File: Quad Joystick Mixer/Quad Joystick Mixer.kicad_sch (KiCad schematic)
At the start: 18 parts, among them J1 Conn_01x02_Pin, U1 LM338-TO-220, U2 LM2990SX-12

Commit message: workign on draft of PSU circuit--thinking about making it onto its own board
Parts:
- removed J1: Conn_01x02_Pin, symbol Connector:Conn_01x02_Pin
- added C10, C11, C9: 2200uF, symbol Device:C_Polarized_US
- added C12: 10uF, symbol Device:C_Polarized_US
- added C13: 0.1uF, symbol Device:C
- added C8: 2220uF, symbol Device:C_Polarized_US
- added D5, D6, D7: B350, Diode_SMD:D_SMC, symbol Diode:B350
- added J1: Barrel_Jack_Switch, Eyewool Connectors:Love My Switches 2.1MM PCB Mount DC Jack, symbol Connector:Barrel_Jack_Switch
- added R5, R6: 10k, symbol Device:R_US
- added SW1: SW_SPST, symbol Switch:SW_SPST
- C7: value C -> 0.1uF
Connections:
- net +12V: now also D7.1 (K), R6.1
- net Earth: now also C1.1, C10.1, C11.1, C12.1, C13.2, C8.2, C9.2, D6.1 (K), D7.2 (A), J1.1, R5.2, R6.2; no longer C1.2
- net at D1.1 (K), D4.2 (A): now also SW1.2 (B)
- net at D1.2 (A), R2.1: now also C10.2, C11.2
- net at C2.1, R2.2, U2.2 (IN): now also C1.2, D5.2 (A); no longer C1.1
- net -12V: now reaches U2.3 (OUT)
- net -12V: now also C12.2, C13.1, D5.1 (K), D6.2 (A), R5.1
- net at D4.1 (K), R1.1: now also C8.1, C9.1
- new net: J1.2, SW1.1 (A)
- no-connect marks 0 -> 1
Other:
- note removed: "todo: verify input connector"
- moved on the sheet: C1, C2, C3, C4, C5, C6, C7, D1, D2, D3, D4, R1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

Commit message: progress on PSU layout
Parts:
- removed C12, C5, C6: 10uF, symbol Device:C_Polarized_US
- removed SW1: SW_SPST, symbol Switch:SW_SPST
- added C12, C14, C5, C6: 10uF, Capacitor_SMD:C_0805_2012Metric_Pad1.18x1.45mm_HandSolder, symbol Device:C
- added C15, C19, C20, C21, C22, C23: 0.1uF, Capacitor_SMD:C_0805_2012Metric_Pad1.18x1.45mm_HandSolder, symbol Device:C
- added C16: 100pF, Capacitor_SMD:C_0805_2012Metric_Pad1.18x1.45mm_HandSolder, symbol Device:C
- added C17, C18: 22uF, Capacitor_SMD:C_1206_3216Metric_Pad1.33x1.80mm_HandSolder, symbol Device:C
- added D10, D8, D9: LED, LED_THT:LED_D3.0mm_FlatTop, symbol Device:LED
- added F1, F2, F3: Polyfuse, Fuse:Fuse_1206_3216Metric_Pad1.42x1.75mm_HandSolder, symbol Device:Polyfuse
- added J1: B6B-XH-A, Eyewool Connectors:B6B-XH-A, symbol Connector:Conn_01x06_Pin
- added L1: 10uH, Inductor_SMD:L_Abracon_ASPI-0630LR, symbol Device:L
- added L2, L3, L4: L_Ferrite, Inductor_SMD:L_0805_2012Metric_Pad1.15x1.40mm_HandSolder, symbol Device:L_Ferrite
- added R10, R9: 0.5R, Resistor_SMD:R_2512_6332Metric_Pad1.40x3.35mm_HandSolder, symbol Device:R_US
- added R11, R12: 10k, Resistor_SMD:R_0805_2012Metric_Pad1.20x1.40mm_HandSolder, symbol Device:R_US
- added R13: 300, Resistor_SMD:R_0805_2012Metric_Pad1.20x1.40mm_HandSolder, symbol Device:R_US
- added R7: 157k, Resistor_SMD:R_0805_2012Metric_Pad1.20x1.40mm_HandSolder, symbol Device:R_US
- added R8: 30k, Resistor_SMD:R_0805_2012Metric_Pad1.20x1.40mm_HandSolder, symbol Device:R_US
- added SW1: SW_DPDT_x2, Eyewool Switches:Taiway DPDT, symbol Switch:SW_DPDT_x2
- added U3: AP63200WU, Package_TO_SOT_SMD:TSOT-23-6, symbol Regulator_Switching:AP63200WU
- C1, C3: footprint (none) -> Capacitor_THT:CP_Radial_D8.0mm_P3.50mm; DK PN (none) -> 1189-2327-ND; MPN (none) -> 50ZLH100MEFC8X11.5
- C10, C11, C9: footprint (none) -> Capacitor_THT:C_Radial_D16.0mm_H25.0mm_P7.50mm; DK PN (none) -> 1189-2266-ND; MPN (none) -> 35ZLH2200MEFC16X25
- C13, C7: footprint (none) -> Capacitor_SMD:C_0805_2012Metric_Pad1.18x1.45mm_HandSolder; DK PN (none) -> 1276-1003-1-ND; MPN (none) -> CL21B104KBCNNNC
- C2, C4: footprint (none) -> Capacitor_SMD:C_0805_2012Metric_Pad1.18x1.45mm_HandSolder; DK PN (none) -> 1276-1029-1-ND; MPN (none) -> CL21B105KBFNNNE
- C8: value 2220uF -> 2200uF; footprint (none) -> Capacitor_THT:C_Radial_D16.0mm_H25.0mm_P7.50mm; DK PN (none) -> 1189-2266-ND; MPN (none) -> 35ZLH2200MEFC16X25
- D1, D2, D3, D4, D5, D6, D7: footprint Diode_SMD:D_SMC -> Diode_SMD:D_SMA_Handsoldering; DK PN (none) -> B350A-FDICT-ND; MPN (none) -> B350A-13-F
- R1, R2: value 1R -> 0.5R; footprint (none) -> Resistor_SMD:R_2512_6332Metric_Pad1.40x3.35mm_HandSolder; DK PN (none) -> CSRN2512FKR500CT-ND; MPN (none) -> CSRN2512FKR500
- R3, R4, R5, R6: footprint (none) -> Resistor_SMD:R_0805_2012Metric_Pad1.20x1.40mm_HandSolder
- U2: value LM2990SX-12 -> LM2990T-12/NOPB; footprint (none) -> Package_TO_SOT_THT:TO-220-3_Vertical
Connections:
- net +12V: now also C14.1, C15.1, C5.1, L4.1, U3.2 (EN), U3.3 (IN)
- net -12V: now also C12.1, L2.1
- net Earth: now also C12.2, C14.2, C15.2, C17.2, C18.2, C19.2, C21.2, C22.2, C23.2, C5.2, C6.2, J1.2 (Pin_2), J1.4 (Pin_4), J1.6 (Pin_6), R11.2, R12.2, R13.2, R8.2, U3.4 (GND)
- net at D1.1 (K), D4.2 (A): now also SW1.1 (A), SW1.4 (A)
- net at C10.2, C11.2, R2.1: now also R10.2; no longer D1.2 (A)
- net at D3.2 (A), R3.2, R4.1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: now also C6.1
- net at J1.2: now also SW1.2 (B), SW1.5 (B)
- net at C8.1, C9.1, R1.1: now also R9.2; no longer D4.1 (K)
- new net: D1.2 (A), R10.1
- new net: D8.1 (K), R11.1
- new net: C16.2, R7.2, R8.1, U3.1 (FB)
- new net: D4.1 (K), R9.1
- new net: C23.1, F3.1, L4.2
- new net: D8.2 (A), F3.2, J1.5 (Pin_5)
- new net: C20.2, L1.1, U3.5 (SW)
- new net: C20.1, U3.6 (BST)
- new net: C21.1, F1.1, L2.2
- new net: C22.1, F2.1, L3.2
- new net: D9.2 (A), F2.2, J1.3 (Pin_3)
- new net: D10.1 (K), F1.2, J1.1 (Pin_1)
- new net: D10.2 (A), R12.1
- new net: D9.1 (K), R13.1
- new net +5V: C16.1, C17.1, C18.1, C19.1, L1.2, L3.1, R7.1
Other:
- moved on the sheet: C1, C10, C11, C13, C2, C3, C4, C7, C8, C9, D1, D2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

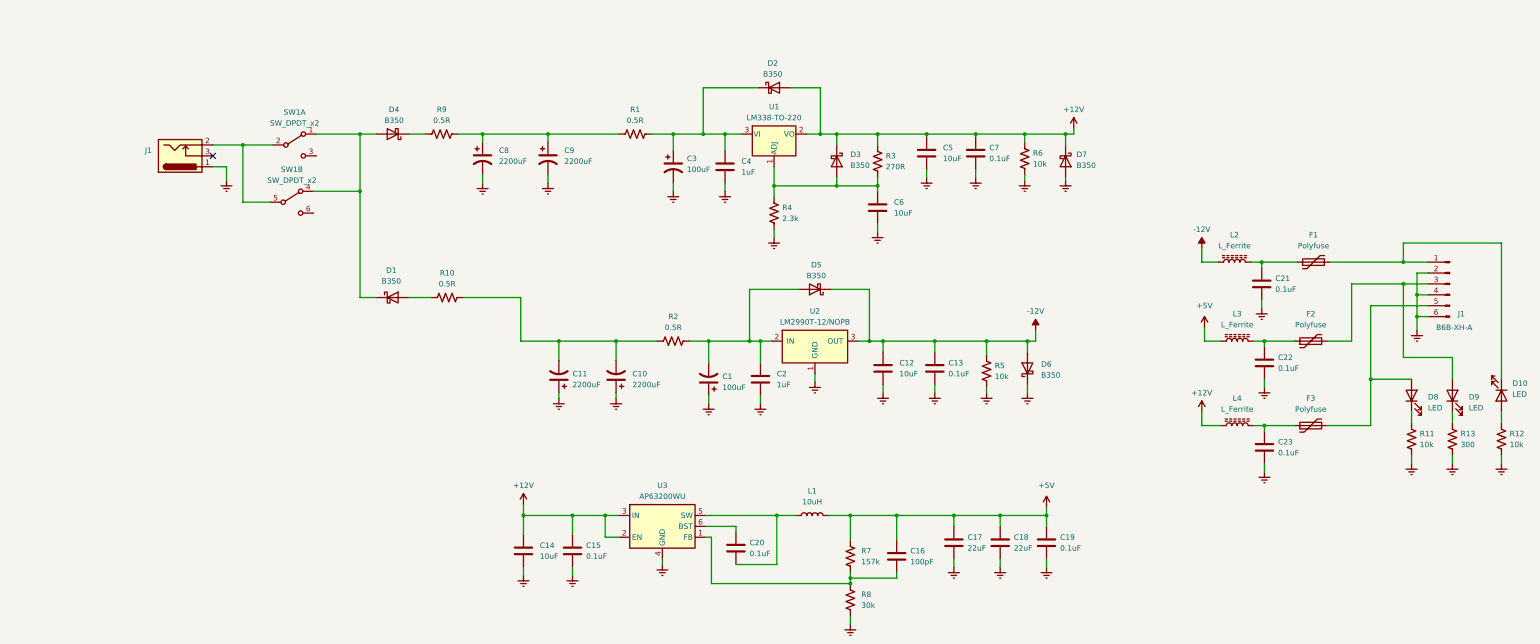
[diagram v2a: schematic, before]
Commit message: clean up power supply schematic
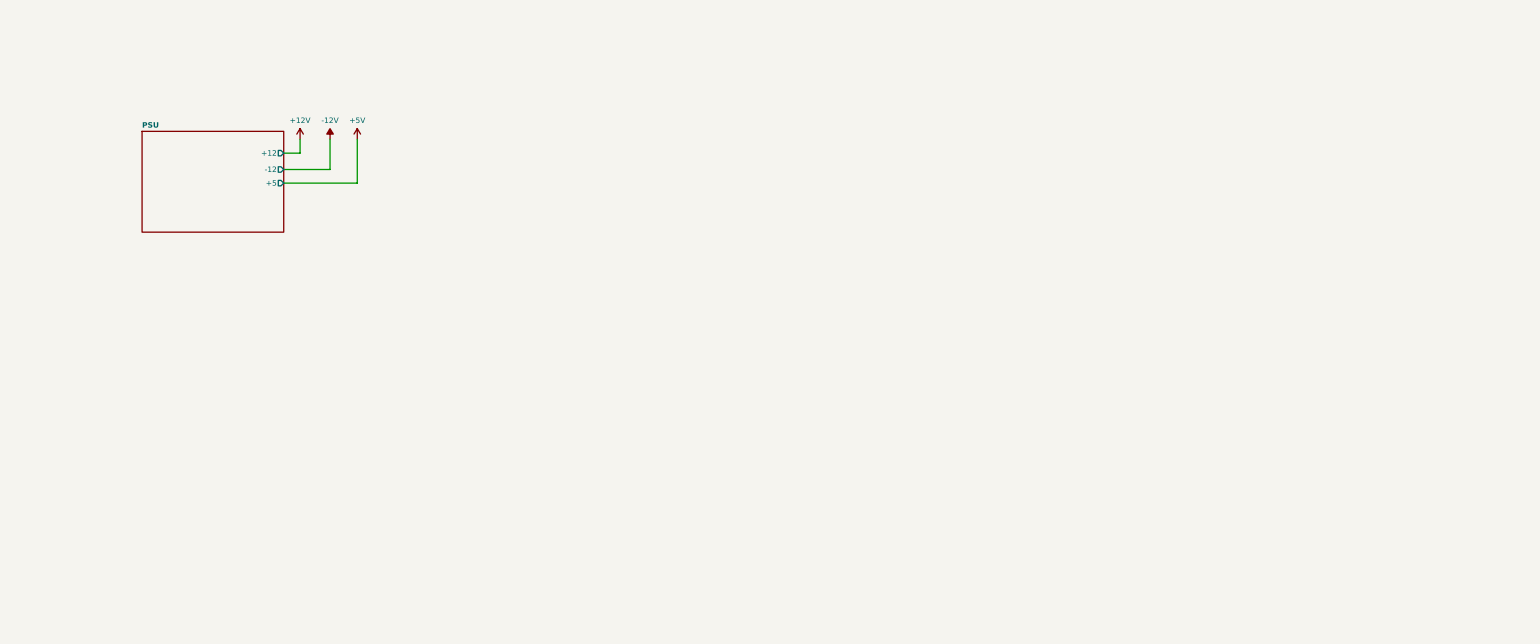
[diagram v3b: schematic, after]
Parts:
- removed C1, C3: 100uF, Capacitor_THT:CP_Radial_D8.0mm_P3.50mm, symbol Device:C_Polarized_US
- removed C10, C11, C8, C9: 2200uF, Capacitor_THT:C_Radial_D16.0mm_H25.0mm_P7.50mm, symbol Device:C_Polarized_US
- removed C12, C14, C5, C6: 10uF, Capacitor_SMD:C_0805_2012Metric_Pad1.18x1.45mm_HandSolder, symbol Device:C
- removed C13, C15, C19, C20, C21, C22, C23, C7: 0.1uF, Capacitor_SMD:C_0805_2012Metric_Pad1.18x1.45mm_HandSolder, symbol Device:C
- removed C16: 100pF, Capacitor_SMD:C_0805_2012Metric_Pad1.18x1.45mm_HandSolder, symbol Device:C
- removed C17, C18: 22uF, Capacitor_SMD:C_1206_3216Metric_Pad1.33x1.80mm_HandSolder, symbol Device:C
- removed C2, C4: 1uF, Capacitor_SMD:C_0805_2012Metric_Pad1.18x1.45mm_HandSolder, symbol Device:C
- removed D1, D2, D3, D4, D5, D6, D7: B350, Diode_SMD:D_SMA_Handsoldering, symbol Diode:B350
- removed D10, D8, D9: LED, LED_THT:LED_D3.0mm_FlatTop, symbol Device:LED
- removed F1, F2, F3: Polyfuse, Fuse:Fuse_1206_3216Metric_Pad1.42x1.75mm_HandSolder, symbol Device:Polyfuse
- removed J1: B6B-XH-A, Eyewool Connectors:B6B-XH-A, symbol Connector:Conn_01x06_Pin
- removed J1: Barrel_Jack_Switch, Eyewool Connectors:Love My Switches 2.1MM PCB Mount DC Jack, symbol Connector:Barrel_Jack_Switch
- removed L1: 10uH, Inductor_SMD:L_Abracon_ASPI-0630LR, symbol Device:L
- removed L2, L3, L4: L_Ferrite, Inductor_SMD:L_0805_2012Metric_Pad1.15x1.40mm_HandSolder, symbol Device:L_Ferrite
- removed R1, R10, R2, R9: 0.5R, Resistor_SMD:R_2512_6332Metric_Pad1.40x3.35mm_HandSolder, symbol Device:R_US
- removed R11, R12, R5, R6: 10k, Resistor_SMD:R_0805_2012Metric_Pad1.20x1.40mm_HandSolder, symbol Device:R_US
- removed R13: 300, Resistor_SMD:R_0805_2012Metric_Pad1.20x1.40mm_HandSolder, symbol Device:R_US
- removed R3: 270R, Resistor_SMD:R_0805_2012Metric_Pad1.20x1.40mm_HandSolder, symbol Device:R_US
- removed R4: 2.3k, Resistor_SMD:R_0805_2012Metric_Pad1.20x1.40mm_HandSolder, symbol Device:R_US
- removed R7: 157k, Resistor_SMD:R_0805_2012Metric_Pad1.20x1.40mm_HandSolder, symbol Device:R_US
- removed R8: 30k, Resistor_SMD:R_0805_2012Metric_Pad1.20x1.40mm_HandSolder, symbol Device:R_US
- removed SW1: SW_DPDT_x2, Eyewool Switches:Taiway DPDT, symbol Switch:SW_DPDT_x2
- removed U1: LM338-TO-220, Package_TO_SOT_THT:TO-220-3_Vertical, symbol Eyewool ICs:LM338-TO-220
- removed U2: LM2990T-12/NOPB, Package_TO_SOT_THT:TO-220-3_Vertical, symbol Regulator_Linear:LM2990SX-12
- removed U3: AP63200WU, Package_TO_SOT_SMD:TSOT-23-6, symbol Regulator_Switching:AP63200WU
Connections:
- no-connect marks 1 -> 0
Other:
- added sheet PSU (PSU.kicad_sch)
